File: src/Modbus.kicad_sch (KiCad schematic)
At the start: 7 parts, among them U2 SP3485

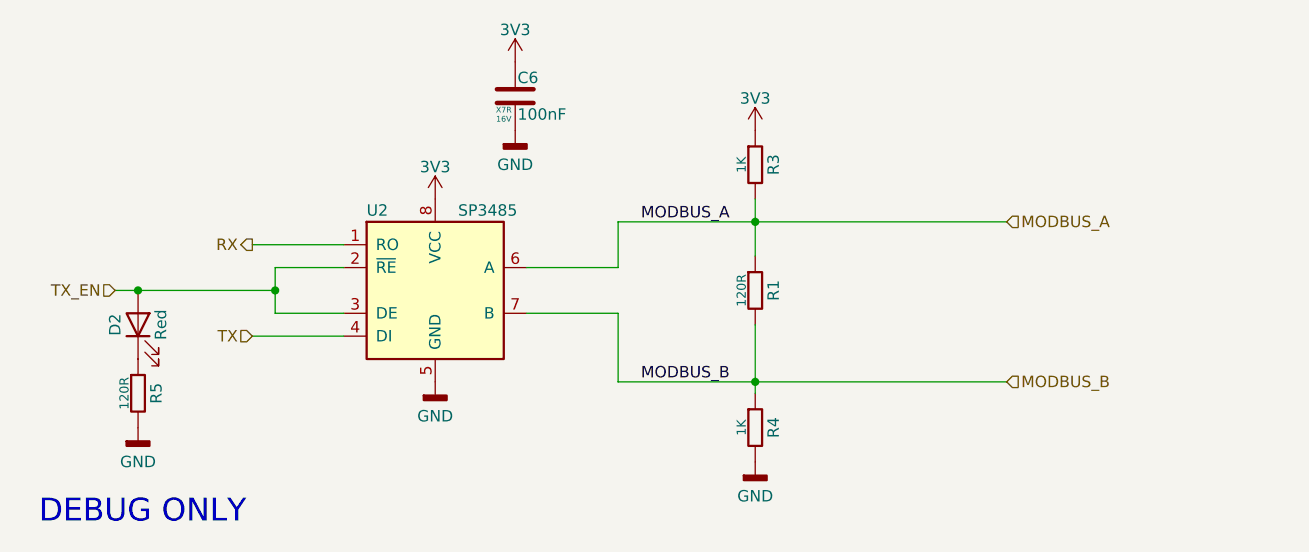
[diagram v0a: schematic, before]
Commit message: V3.1 first changes
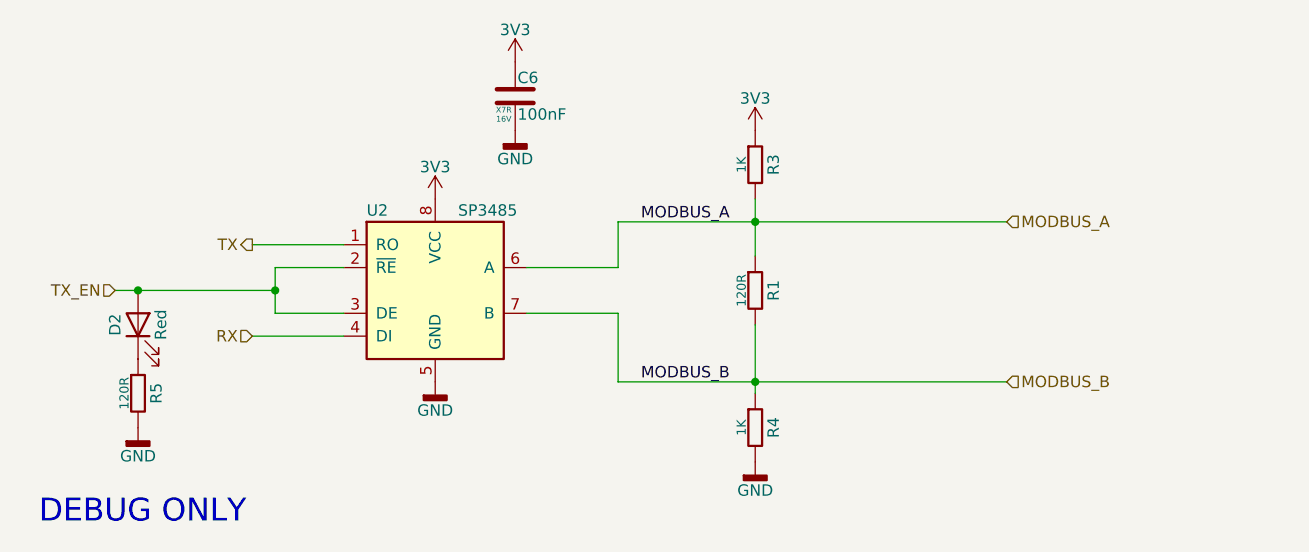
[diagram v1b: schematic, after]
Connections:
- net RX: now also U2.4 (DI); no longer U2.1 (RO)
- net TX: now also U2.1 (RO); no longer U2.4 (DI)

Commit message: ongoing work
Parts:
- removed R5: 120R, 7Sigma:R_0402_1005Metric, symbol Resistor:0402WGF1200TCE
- added R5: 1K, 7Sigma:R_0402_1005Metric, symbol Resistor:0402WGF1001TCE
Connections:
- net GND: now also R5.2
- net at D2.1 (K): now also R5.1
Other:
- note removed: "DEBUG ONLY"

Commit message: Layout progress
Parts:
- C6: Price @1 USD (none) -> 0.0015; Price @100 USD (none) -> 0.0015; Price @Bulk USD (none) -> 0.0012; Price Bulk Qty (none) -> 1000; Price Source (none) -> LCSC; Price Updated (none) -> 2026-05-14
- D2: Price @1 USD (none) -> 0.0396; Price @100 USD (none) -> 0.0396; Price @Bulk USD (none) -> 0.0266; Price Bulk Qty (none) -> 600; Price Source (none) -> LCSC; Price Updated (none) -> 2026-05-14
- R1, R3, R4, R5: Price @1 USD (none) -> 0.0011; Price @100 USD (none) -> 0.0011; Price @Bulk USD (none) -> 0.0009; Price Bulk Qty (none) -> 1000; Price Source (none) -> LCSC; Price Updated (none) -> 2026-05-14
- U2: Price @1 USD (none) -> 0.3077; Price @100 USD (none) -> 0.2063; Price @Bulk USD (none) -> 0.1685; Price Bulk Qty (none) -> 1000; Price Source (none) -> LCSC; Price Updated (none) -> 2026-05-14

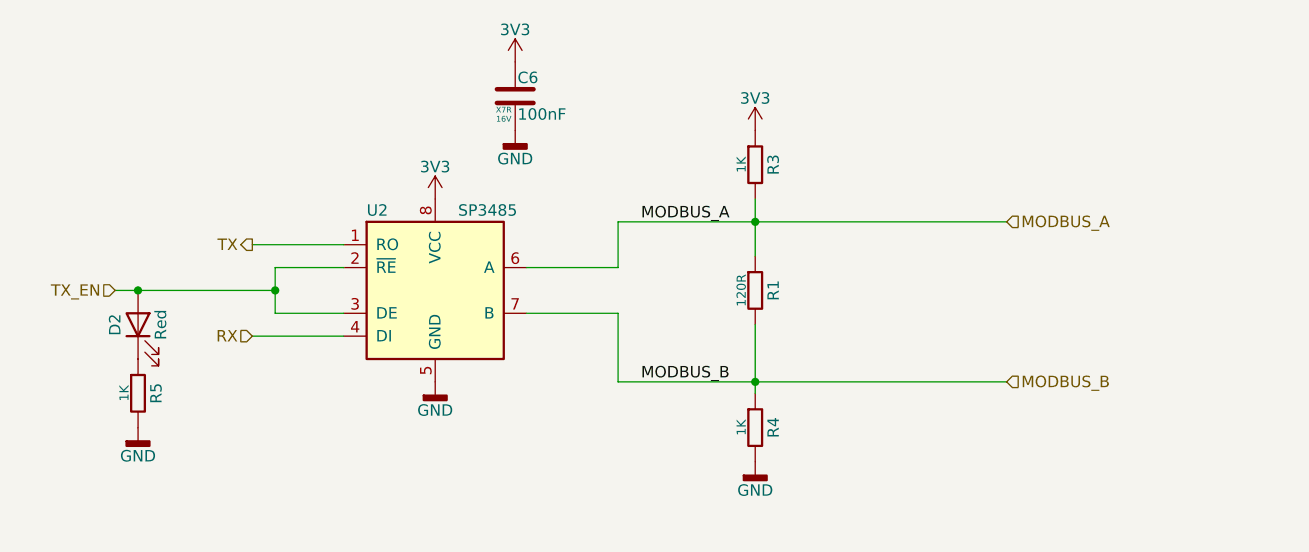
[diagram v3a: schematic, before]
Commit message: schematic cleanup, verification. GPIO9 pin pulldown changed to pullup.
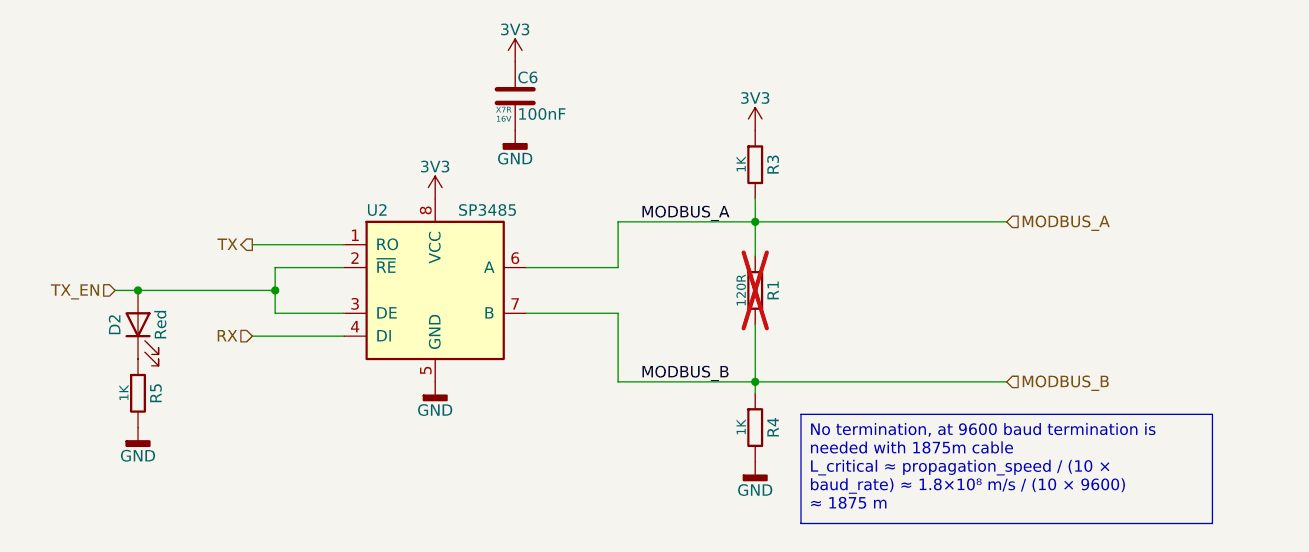
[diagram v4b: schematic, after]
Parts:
- R1: now not fitted
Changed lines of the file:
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@@
 	(generator_version "10.0")
 	(paper "A4")
+	(text_box "No termination, at 9600 baud termination is needed with 1875m cable\nL_critical ≈ propagation_speed / (10 × baud_rate) ≈ 1.8×10⁸ m/s / (10 × 9600) ≈ 1875 m"
+		(exclude_from_sim no)
+		(at 109.22 82.3486 0)
+		(size 45.72 12.1268)
+		(margins 0.9525 0.9525 0.9525 0.9525)
+		(stroke
+			(width 0)
+			(type solid)
+		)
+		(fill
+			(type none)
+		)
+		(effects
+			(font
+				(size 1.27 1.27)
+			)
+			(justify left top)
+		)
+	)
 	(junction
 		(at 50.8 68.58)
@@
 		(on_board yes)
 		(in_pos_files yes)
-		(dnp no)
+		(dnp yes)
 		(property "Reference" "R1"
 			(at 106.172 68.58 90)
